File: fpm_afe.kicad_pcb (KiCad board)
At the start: 2 copper layers, 63.5 x 76 mm, 36 parts, among them J1 39301022, J2 132134, J3 132134, J4 878311420, U1 TPS7A4700xRGW, U2 PE43713B-Z, U3 ADL5536, U4 LFCN-800+, U5 LFCN-800+, U6 PAT-3+

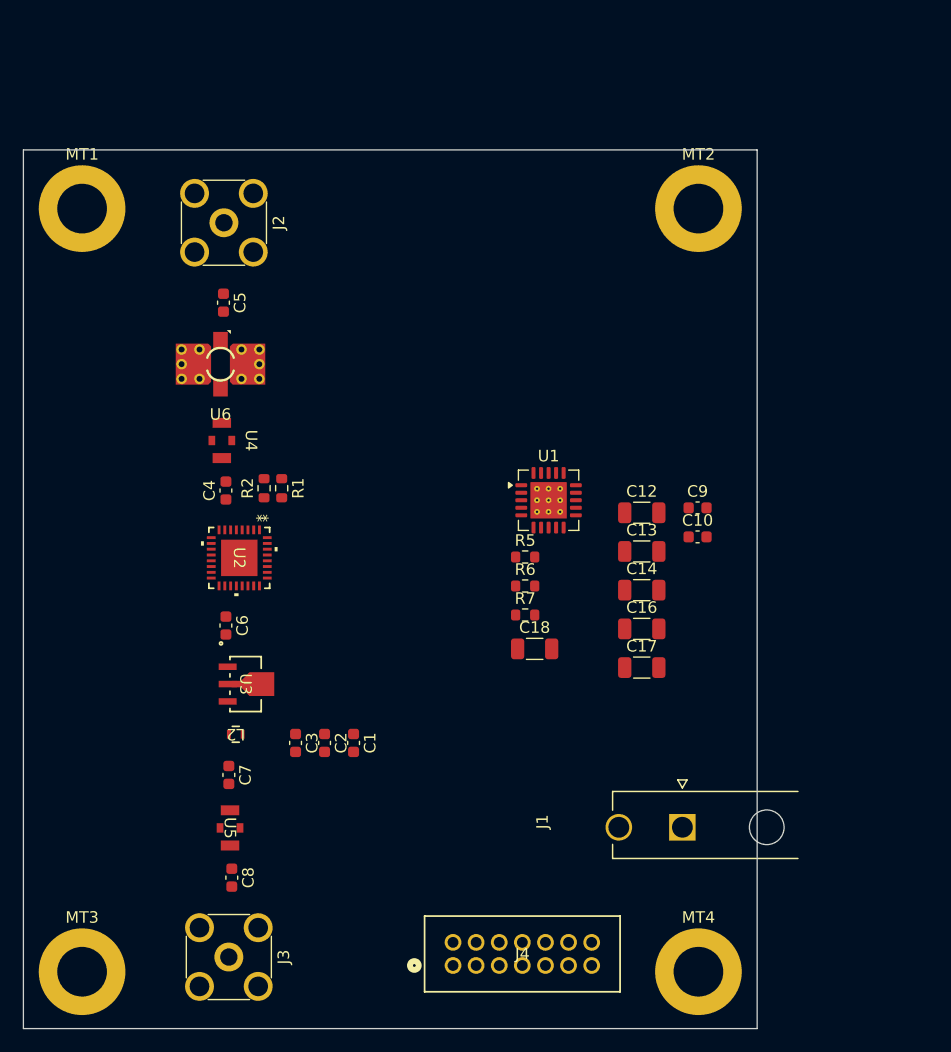
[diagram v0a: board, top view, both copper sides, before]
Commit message: Finish schematic
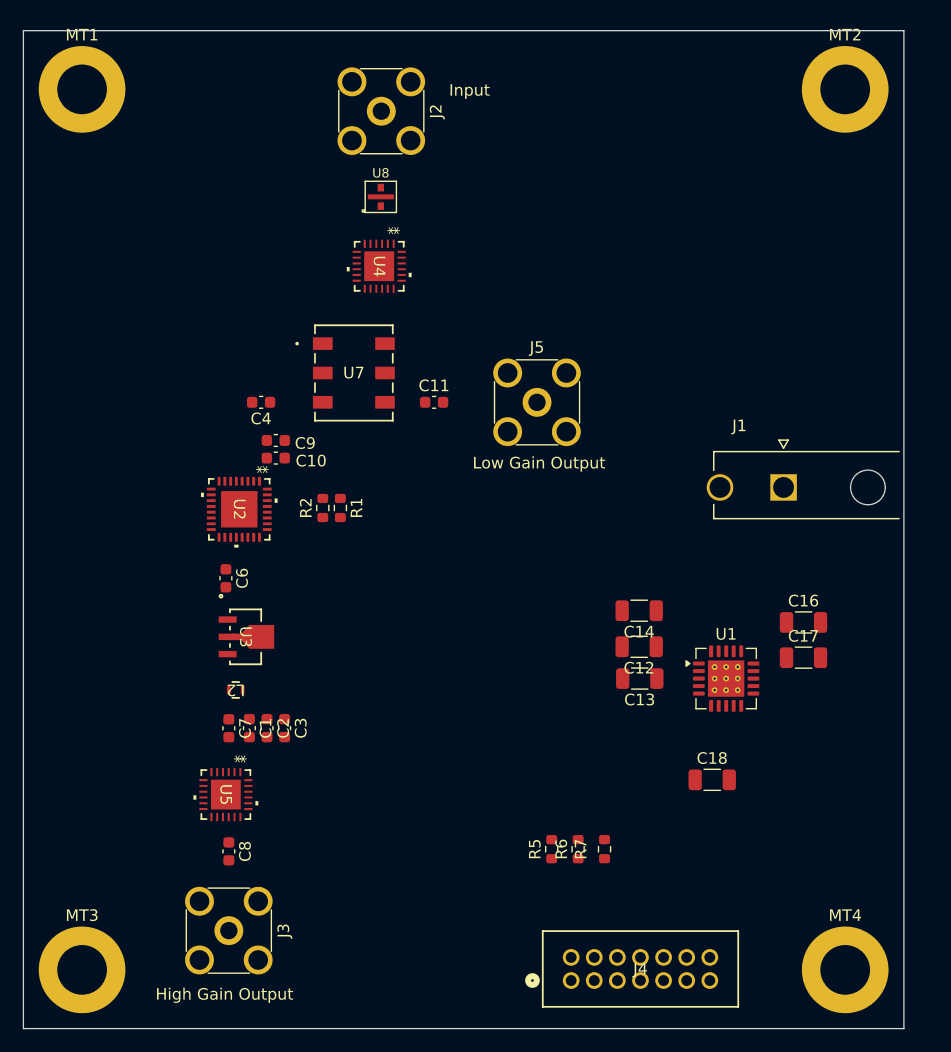
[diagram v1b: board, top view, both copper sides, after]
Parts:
- removed C5: 0.1u, Capacitor_SMD:C_0603_1608Metric
- removed U6: PAT-3+, My_Footprints:Mini-Circuits_PAT-0plus_AF320_PL208
- added C11: 0.1u, Capacitor_SMD:C_0603_1608Metric, F.Cu at (160.0, 59.9)
- added J5: 132134, My_Footprints:SMA_Amphenol_132134_Vertical, F.Cu at (168.9, 59.9)
- added U7: RPS-2-30+, My_Footprints:TT1413_MNC, F.Cu at (153.1, 57.4)
- added U8: RCAT-01+, My_Footprints:RCAT_LZ1737, F.Cu at (155.4, 42.2)
- L2: value 0603LS-471XJLC -> 43nH
- U3: value ADL5536 -> ADL5611
- U4, U5: value LFCN-800+ -> XLF-172H+; footprint My_Footprints:FV1206_MNC -> My_Footprints:QFN24_XLF-13H&plus__MNC
- moved C10 37.1 mm to (146.3, 64.8), turned to 180 degrees
- moved C9 37.0 mm to (146.3, 63.2), turned to 180 degrees
- moved J1 30.7 mm to (190.2, 67.3)
- moved R5 25.4 mm to (170.2, 98.6), turned to 90 degrees
- moved R6 23.2 mm to (172.5, 98.6), turned to 90 degrees
- moved U1 21.8 mm to (185.3, 83.8)
- moved R7 21.4 mm to (174.8, 98.6), turned to 90 degrees
- moved U4 20.3 mm to (155.3, 48.2)
- moved C18 19.1 mm to (184.1, 92.6)
- moved J2 16.7 mm to (155.4, 34.8)
- moved MT2 16.4 mm to (195.6, 32.9)
- moved C17 14.0 mm to (192.0, 82.0)
- moved C16 14.0 mm to (192.0, 79.0)
- moved MT4 12.7 mm to (195.6, 109.1)
- moved C12 11.6 mm to (177.8, 81.1), turned to 180 degrees
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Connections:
- C4 pad 1: Net-(U4-RF_OUT) -> Net-(U7-PORT_2)
- C7 pad 2: Net-(U5-RF_IN) -> Net-(U5-RF-IN)
- C8 pad 1: Net-(U5-RF_OUT) -> Net-(U5-RF-OUT)
- U4 pad 1: Net-(U4-RF_IN) -> GND
- U4 pad 3: Net-(U4-RF_OUT) -> Net-(U4-RF-IN)
- U5 pad 1: Net-(U5-RF_IN) -> GND
- U5 pad 3: Net-(U5-RF_OUT) -> Net-(U5-RF-IN)
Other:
- board size 63.5 x 76 mm -> 76.2 x 86.4 mm
- board text added: "High Gain Output"
- board text added: "Input"
- board text added: "Low Gain Output"

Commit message: Board finished, gerbers generated
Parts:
- added G***: LOGO, myparts:bnl_logo, F.Cu at (178.3, 44.6)
- J2, J3, J5: value 132134 -> TMB-V5F2-3LC; footprint My_Footprints:SMA_Amphenol_132134_Vertical -> My_Footprints:TMB-V5F2-3LC_PCBWay1_GCPW
- moved J1 29.4 mm to (190.3, 96.7)
- moved C18 15.9 mm to (194.6, 80.7), turned to -90 degrees
- moved C14 10.9 mm to (186.9, 72.1), turned to 90 degrees
- moved C9 10.8 mm to (150.1, 73.4)
- moved MT1 10.3 mm to (129.5, 43.2)
- moved MT2 10.3 mm to (195.6, 43.2)
- moved R1 8.99 mm to (151.9, 78.1)
- moved R2 8.99 mm to (150.4, 78.1)
- moved J2 8.99 mm to (155.4, 43.7), turned to 0 degrees
- moved J5 8.80 mm to (167.2, 68.6), turned to -90 degrees
- moved C4 8.71 mm to (146.5, 68.5)
- moved U7 8.64 mm to (152.7, 66.0)
- moved C11 8.63 mm to (159.7, 68.6)
- moved U4 8.61 mm to (155.2, 56.8)
- moved U8 8.36 mm to (155.4, 50.5), turned to 180 degrees
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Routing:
- net /atten_si: track 0.00 -> 45.1 mm, vias 0 -> 2
- net /atten_clk: track 0.00 -> 38.4 mm, vias 0 -> 2
- net /atten_le: track 0.00 -> 34.7 mm, vias 0 -> 2
- net GND: track 0.00 -> 22.3 mm, vias 0 -> 90
- net Net-(U2-*P/S): track 0.00 -> 13.6 mm, vias 0 -> 2
- net Net-(J4-Pad1): track 0.00 -> 10.7 mm
- net Net-(J4-Pad3): track 0.00 -> 10.6 mm
- net Net-(J4-Pad5): track 0.00 -> 10.5 mm
- net +5.0V: track 0.00 -> 7.35 mm, vias 0 -> 8
- net Net-(C7-Pad1): track 0.00 -> 6.07 mm
- net Net-(J2-In): track 0.00 -> 6.00 mm
- net Net-(J5-In): track 0.00 -> 5.35 mm
- net Net-(U2-RF1): track 0.00 -> 5.20 mm
- net Net-(U4-RF-OUT): track 0.00 -> 4.78 mm
- net Net-(U4-RF-IN): track 0.00 -> 3.52 mm
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- added copper zone on F.Cu, net +5.0V
- added copper zone on In2.Cu, net +5.0V
- added copper zone on F.Cu, net /+12v
- added copper zone on In2.Cu, net /+12v
- added copper zone on B.Cu, net GND
- added copper zone on F.Cu, net GND
- added copper zone on In1.Cu, net GND
- added copper zone on In4.Cu, net GND
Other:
- board size 76.2 x 86.4 mm -> 76.2 x 76.2 mm
- copper layers 2 -> 6
- board text added: "0.0175"
- board text added: "0.0350"
- board text added: "0.1195"
- board text added: "0.1750"
- board text added: "0.4300"
- board text added: "1. Use PCBWay standard 6-layer stackup #1 unless otherwise approved."
- board text added: "1.6 mm nominal | 1 oz finished outer Cu | 1 oz inner Cu | 70% inner residual Cu"
- board text added: "2. L2 and L5 are continuous GND reference planes."
- board text added: "2116 RC58%, Dk 4.45"
- board text added: "3. Top-layer RF traces: 50 ohm single-ended, referenced to L2."
- board text added: "4. Fabricator may adjust trace width to achieve 50 ohm +/-10%."
- board text added: "5. Notify engineering before any stackup/material substitution."
- board text added: "6-LAYER PCB STACKUP - PCBWay STANDARD #1"
- board text added: "7628 RC46%, Dk 4.74"
- board text added: "CONTROLLED IMPEDANCE NOTES 1. RF nets identified in the fabrication data shall be 50 Ω ±10% grounded coplanar waveguide, routed on L1 and referenced to L2. 2. Nominal geometry: trace width = [8 mil], coplanar gap = [8 mil]. 3. Impedance shall be calculated using finished copper thickness, finished dielectric thickness, solder-mask presence, and the fabricator's actual material properties. 4. Fabr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"
- board text added: "CORE"
- board text added: "CU"
- board text added: "FAB / IMPEDANCE NOTES"
- board text added: "FR-4 core, Dk 4.6"
- board text added: "GENERAL FABRICATION NOTES 1. Fabricate in accordance with IPC-6012, Class 2, unless otherwise specified. 2. Finished board thickness: 1.60 mm ±10%. 3. Laminate: FR-4, Tg ≥ 150°C. 4. Finished outer-layer copper: 1 oz minimum. 5. Inner-layer copper: 1 oz. 6. Surface finish: ENIG per IPC-4552. 7. Solder mask: both sides, color GREEN. 8. Silkscreen: both sides as supplied, color WHITE. 9. All holes a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"
- board text added: "Inner Cu 1 oz - Power / signal"
- board text added: "Inner Cu 1 oz - SOLID GND"
- board text added: "L1"
- board text added: "L2"
- board text added: "L3"
- board text added: "L4"
- board text added: "L5"
- board text added: "L6"
- board text added: "Layer"
- board text added: "Material / Function"
- board text added: "NSLS-II Fill Pattern Monitor AFE E-SK-2604 Rev 1 9-20-26"
- board text added: "Outer base Cu 0.5 oz; plated to 1 oz"
- board text added: "PP"
- board text added: "Thickness (mm)"
- board text added: "Type"
